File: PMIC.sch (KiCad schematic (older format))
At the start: 63 parts

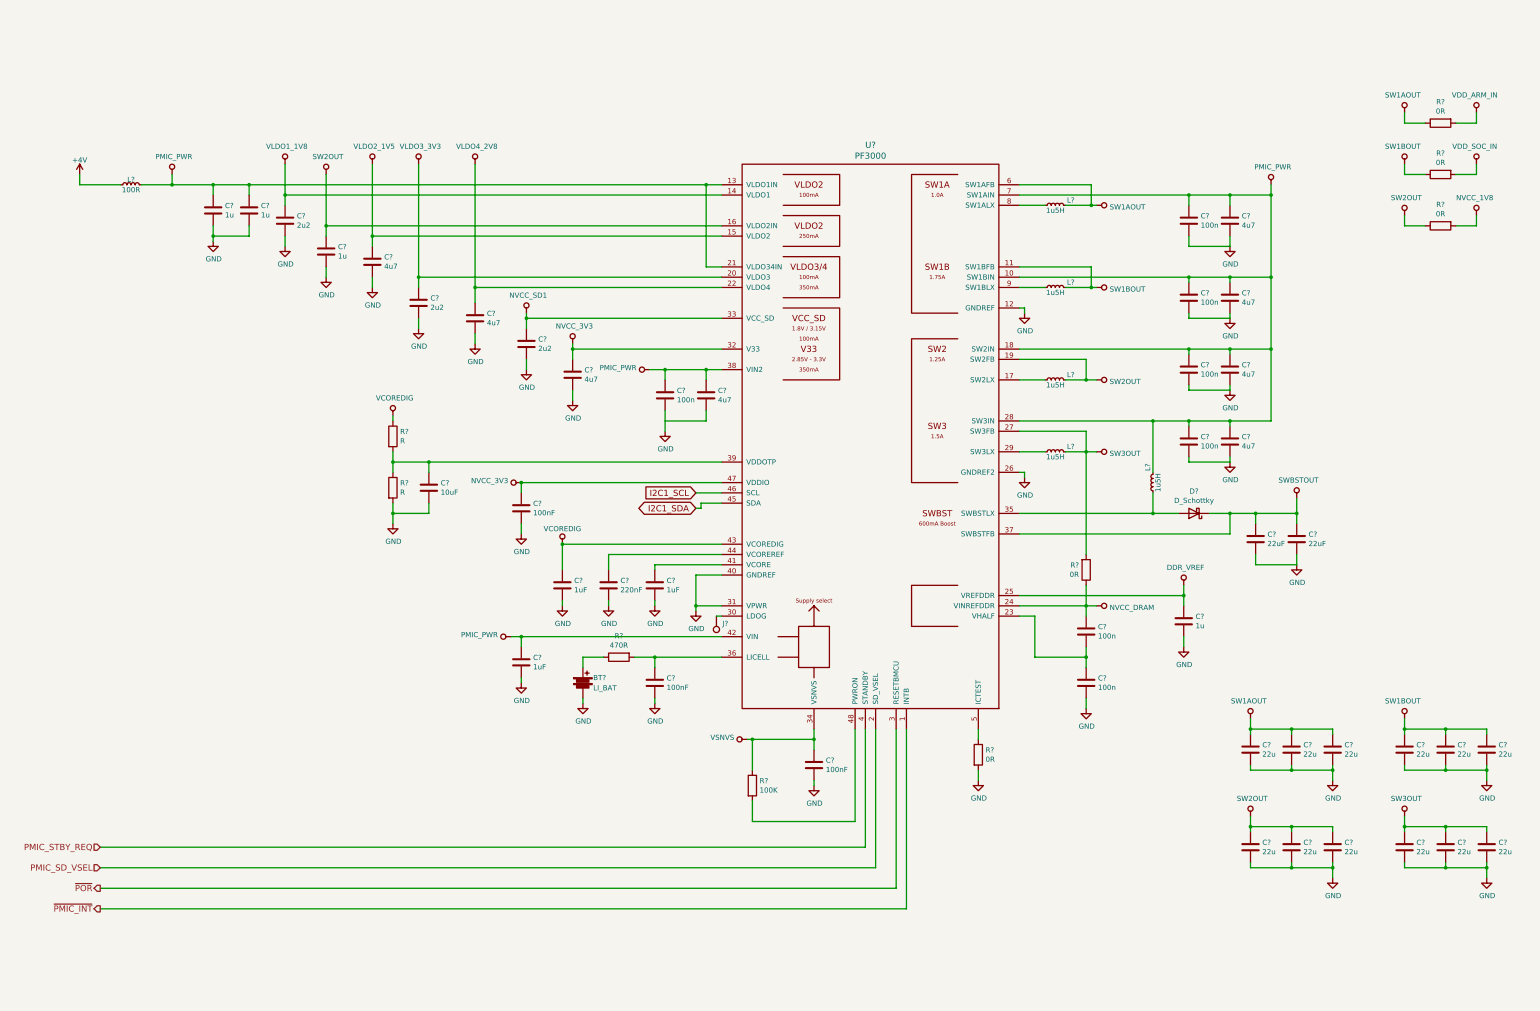
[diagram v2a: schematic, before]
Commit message: Prepare for two battery types NiMH battery for using the original battery pack LiPo battery for using long lasting modern battery
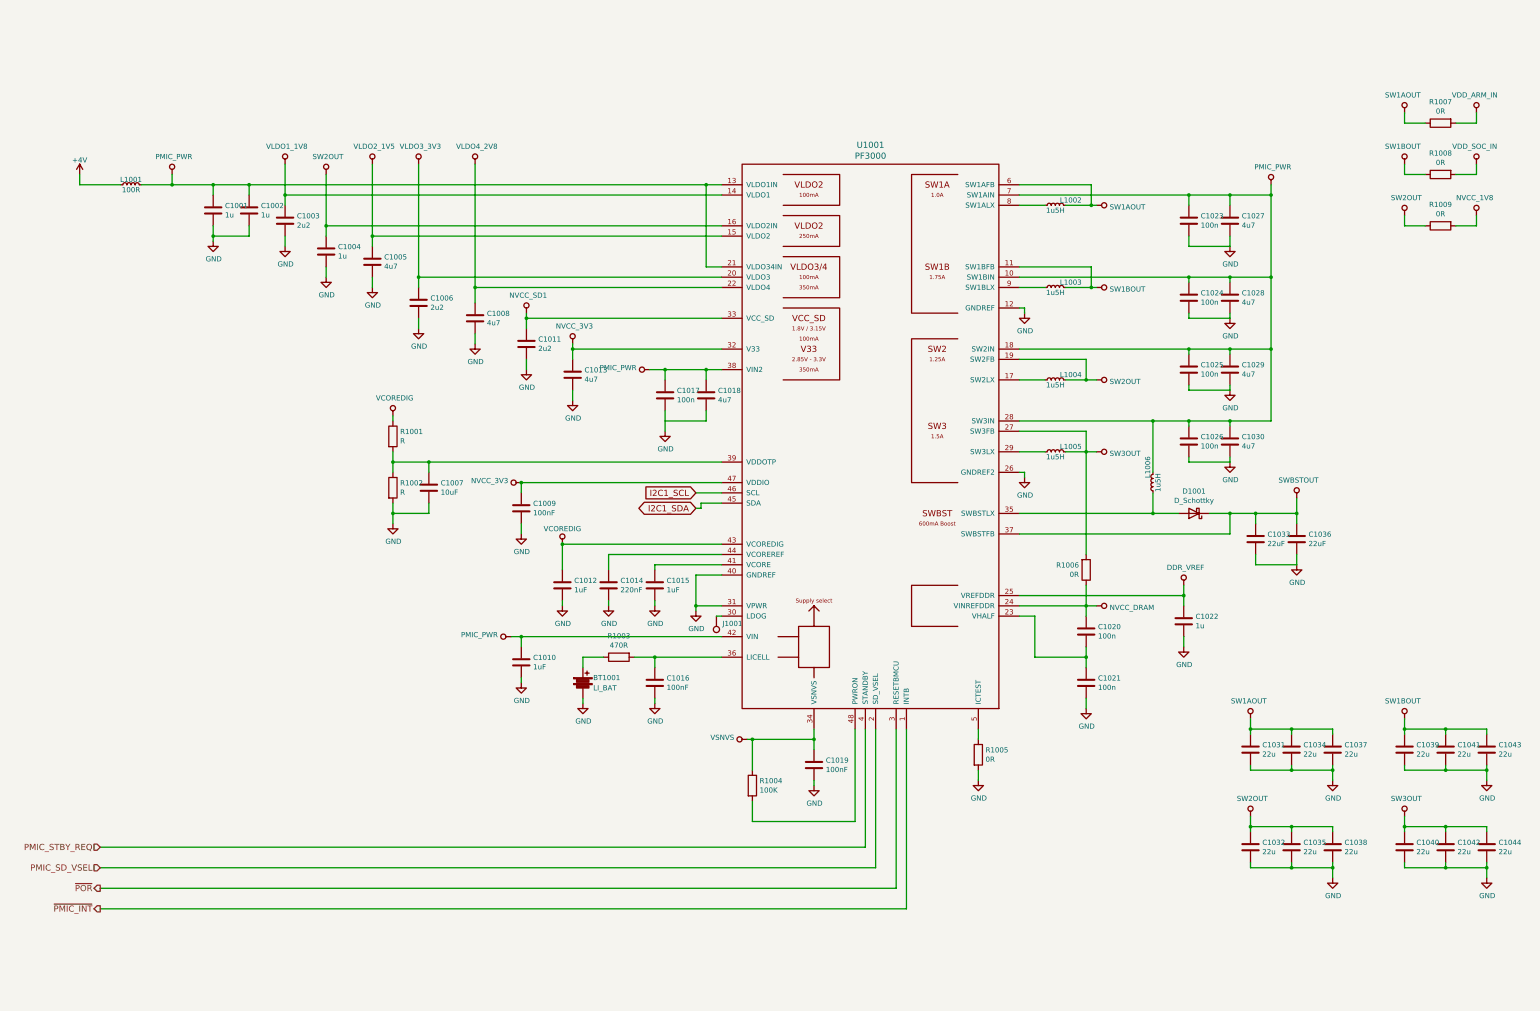
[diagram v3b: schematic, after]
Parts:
- gave numbers to parts that had none: 63

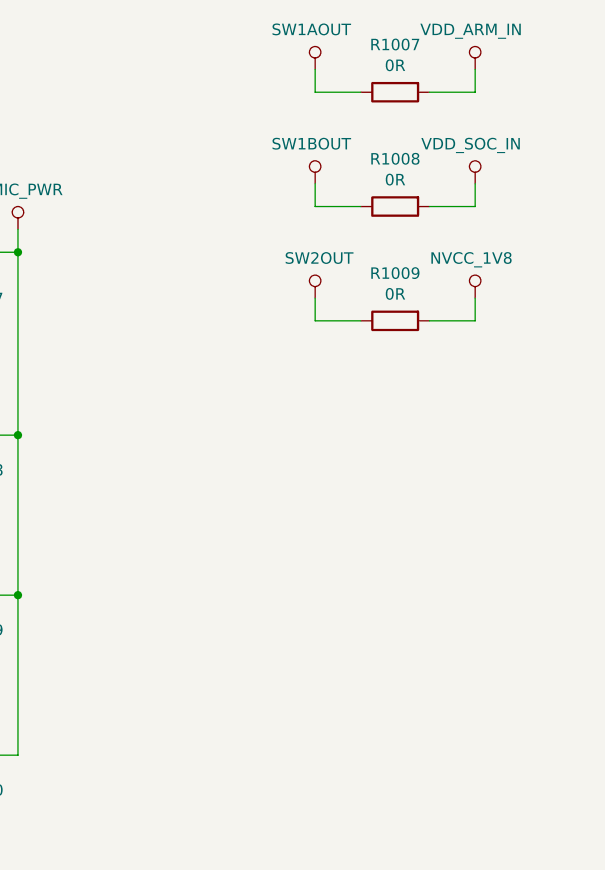
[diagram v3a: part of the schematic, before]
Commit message: Added power domains overview in POWER.sch subsheet fixed some power connections added datasheet for bq24401 charge controller updated schematic library
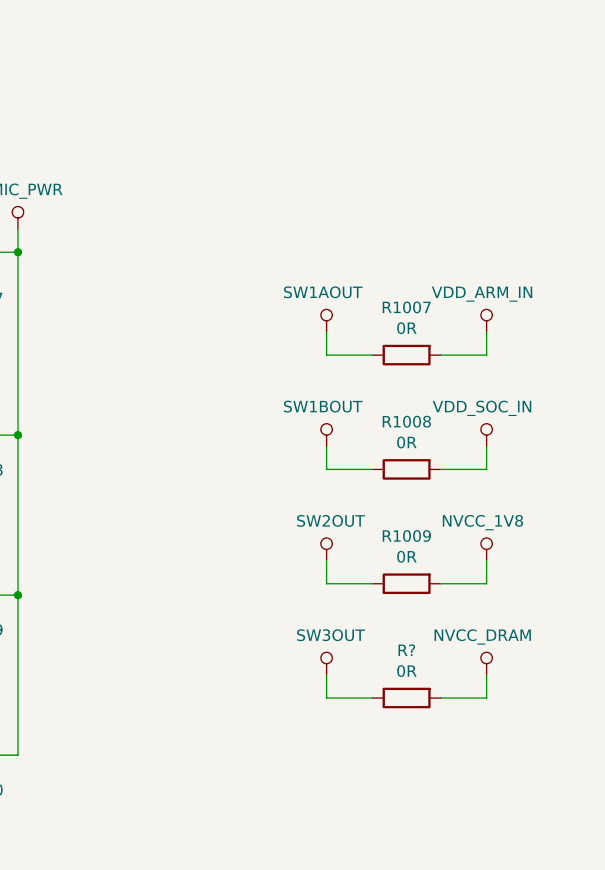
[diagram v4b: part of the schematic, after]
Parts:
- added R?: 0R, symbol R
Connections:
- net NVCC_DRAM: now also R?.2
- net SW3OUT: now also R?.1
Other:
- moved on the sheet: R1007, R1008, R1009
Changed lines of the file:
@@
 L VDD_ARM_IN #PWR1062
 U 1 1 59281B8F
-P 15300 1900
-F 0 "#PWR1062" H 15350 1950 50  0001 C CNN
-F 1 "VDD_ARM_IN" H 15317 2073 50  0000 C CNN
-F 2 "" H 6400 -750 50  0001 C CNN
-F 3 "" H 6400 -750 50  0001 C CNN
-	1    15300 1900
+P 15350 3050
+F 0 "#PWR1062" H 15400 3100 50  0001 C CNN
+F 1 "VDD_ARM_IN" H 15367 3223 50  0000 C CNN
+F 2 "" H 6450 400 50  0001 C CNN
+F 3 "" H 6450 400 50  0001 C CNN
+	1    15350 3050
 	-1   0    0    -1
 $EndComp
@@
 L VDD_SOC_IN #PWR1063
 U 1 1 5928223D
-P 15300 2400
-F 0 "#PWR1063" H 15350 2450 50  0001 C CNN
-F 1 "VDD_SOC_IN" H 15317 2573 50  0000 C CNN
-F 2 "" H 6400 -250 50  0001 C CNN
-F 3 "" H 6400 -250 50  0001 C CNN
-	1    15300 2400
+P 15350 3550
+F 0 "#PWR1063" H 15400 3600 50  0001 C CNN
+F 1 "VDD_SOC_IN" H 15367 3723 50  0000 C CNN
+F 2 "" H 6450 900 50  0001 C CNN
+F 3 "" H 6450 900 50  0001 C CNN
+	1    15350 3550
 	-1   0    0    -1
 $EndComp
@@
 L SW1AOUT #PWR1057
 U 1 1 593E805C
-P 14600 1900
-F 0 "#PWR1057" H 14650 1950 50  0001 C CNN
-F 1 "SW1AOUT" H 14617 2073 50  0000 C CNN
-F 2 "" H 2650 -1150 50  0001 C CNN
-F 3 "" H 2650 -1150 50  0001 C CNN
-	1    14600 1900
+P 14650 3050
+F 0 "#PWR1057" H 14700 3100 50  0001 C CNN
+F 1 "SW1AOUT" H 14667 3223 50  0000 C CNN
+F 2 "" H 2700 0   50  0001 C CNN
+F 3 "" H 2700 0   50  0001 C CNN
+	1    14650 3050
 	-1   0    0    -1
 $EndComp
@@
 L R R1007
 U 1 1 593E86B0
-P 14950 2000
-F 0 "R1007" V 14743 2000 50  0000 C CNN
-F 1 "0R" V 14834 2000 50  0000 C CNN
-F 2 "" V -20 -600 50  0001 C CNN
-F 3 "" H 50  -600 50  0001 C CNN
-	1    14950 2000
+P 15000 3150
+F 0 "R1007" V 14793 3150 50  0000 C CNN
+F 1 "0R" V 14884 3150 50  0000 C CNN
+F 2 "" V 30  550 50  0001 C CNN
+F 3 "" H 100 550 50  0001 C CNN
+	1    15000 3150
 	0    -1   1    0
 $EndComp
 Wire Wire Line
-	14800 2000 14600 2000
-Wire Wire Line
-	14600 2000 14600 1900
-Wire Wire Line
-	15100 2000 15300 2000
-Wire Wire Line
-	15300 2000 15300 1900
+	14850 3150 14650 3150
+Wire Wire Line
+	14650 3150 14650 3050
+Wire Wire Line
+	15150 3150 15350 3150
+Wire Wire Line
+	15350 3150 15350 3050
 Wire Wire Line
 	11550 3400 11550 3600
@@
 L R R1008
 U 1 1 593E95E8
-P 14950 2500
-F 0 "R1008" V 14743 2500 50  0000 C CNN
-F 1 "0R" V 14834 2500 50  0000 C CNN
-F 2 "" V -20 -100 50  0001 C CNN
-F 3 "" H 50  -100 50  0001 C CNN
-	1    14950 2500
+P 15000 3650
+F 0 "R1008" V 14793 3650 50  0000 C CNN
+F 1 "0R" V 14884 3650 50  0000 C CNN
+F 2 "" V 30  1050 50  0001 C CNN
+F 3 "" H 100 1050 50  0001 C CNN
+	1    15000 3650
 	0    -1   1    0
 $EndComp
 Wire Wire Line
-	14800 2500 14600 2500
-Wire Wire Line
-	14600 2500 14600 2400
-Wire Wire Line
-	15100 2500 15300 2500
-Wire Wire Line
-	15300 2500 15300 2400
+	14850 3650 14650 3650
+Wire Wire Line
+	14650 3650 14650 3550
+Wire Wire Line
+	15150 3650 15350 3650
+Wire Wire Line
+	15350 3650 15350 3550
 $Comp
 L SW1BOUT #PWR1058
 U 1 1 593E967C
-P 14600 2400
-F 0 "#PWR1058" H 14650 2450 50  0001 C CNN
-F 1 "SW1BOUT" H 14617 2573 50  0000 C CNN
-F 2 "" H 2900 -1250 50  0001 C CNN
-F 3 "" H 2900 -1250 50  0001 C CNN
-	1    14600 2400
+P 14650 3550
+F 0 "#PWR1058" H 14700 3600 50  0001 C CNN
+F 1 "SW1BOUT" H 14667 3723 50  0000 C CNN
+F 2 "" H 2950 -100 50  0001 C CNN
+F 3 "" H 2950 -100 50  0001 C CNN
+	1    14650 3550
 	-1   0    0    -1
 $EndComp
@@
 L NVCC_1V8 #PWR1064
 U 1 1 593E9AC0
-P 15300 2900
-F 0 "#PWR1064" H 15350 2950 50  0001 C CNN
-F 1 "NVCC_1V8" H 15317 3073 50  0000 C CNN
-F 2 "" H 1300 800 50  0001 C CNN
-F 3 "" H 1300 800 50  0001 C CNN
-	1    15300 2900
+P 15350 4050
+F 0 "#PWR1064" H 15400 4100 50  0001 C CNN
+F 1 "NVCC_1V8" H 15367 4223 50  0000 C CNN
+F 2 "" H 1350 1950 50  0001 C CNN
+F 3 "" H 1350 1950 50  0001 C CNN
+	1    15350 4050
 	-1   0    0    -1
 $EndComp
@@
 L SW2OUT #PWR1059
 U 1 1 593E9BEA
-P 14600 2900
-F 0 "#PWR1059" H 14650 2950 50  0001 C CNN
-F 1 "SW2OUT" H 14617 3073 50  0000 C CNN
-F 2 "" H 2850 -1600 50  0001 C CNN
-F 3 "" H 2850 -1600 50  0001 C CNN
-	1    14600 2900
+P 14650 4050
+F 0 "#PWR1059" H 14700 4100 50  0001 C CNN
+F 1 "SW2OUT" H 14667 4223 50  0000 C CNN
+F 2 "" H 2900 -450 50  0001 C CNN
+F 3 "" H 2900 -450 50  0001 C CNN
+	1    14650 4050
 	1    0    0    -1
 $EndComp
@@
 L R R1009
 U 1 1 593E9DDD
-P 14950 3000
-F 0 "R1009" V 14743 3000 50  0000 C CNN
-F 1 "0R" V 14834 3000 50  0000 C CNN
-F 2 "" V -20 400 50  0001 C CNN
-F 3 "" H 50  400 50  0001 C CNN
-	1    14950 3000
+P 15000 4150
+F 0 "R1009" V 14793 4150 50  0000 C CNN
+F 1 "0R" V 14884 4150 50  0000 C CNN
+F 2 "" V 30  1550 50  0001 C CNN
+F 3 "" H 100 1550 50  0001 C CNN
+	1    15000 4150
 	0    -1   1    0
 $EndComp
 Wire Wire Line
-	14800 3000 14600 3000
-Wire Wire Line
-	14600 3000 14600 2900
-Wire Wire Line
-	15100 3000 15300 3000
-Wire Wire Line
-	15300 3000 15300 2900
+	14850 4150 14650 4150
+Wire Wire Line
+	14650 4150 14650 4050
+Wire Wire Line
+	15150 4150 15350 4150
+Wire Wire Line
+	15350 4150 15350 4050
 $Comp
 L C C1031
@@
 	1    0    0    -1
 $EndComp
+$Comp
+L NVCC_DRAM #PWR?
+U 1 1 5959870A
+P 15350 4550
+F 0 "#PWR?" H 15400 4600 50  0001 C CNN
+F 1 "NVCC_DRAM" H 15367 4723 50  0000 C CNN
+F 2 "" H 1350 2450 50  0001 C CNN
+F 3 "" H 1350 2450 50  0001 C CNN
+	1    15350 4550
+	-1   0    0    -1
+$EndComp
+$Comp
+L SW3OUT #PWR?
+U 1 1 59598710
+P 14650 4550
+F 0 "#PWR?" H 14700 4600 50  0001 C CNN
+F 1 "SW3OUT" H 14667 4723 50  0000 C CNN
+F 2 "" H 2900 50  50  0001 C CNN
+F 3 "" H 2900 50  50  0001 C CNN
+	1    14650 4550
+	1    0    0    -1
+$EndComp
+$Comp
+L R R?
+U 1 1 59598716
+P 15000 4650
+F 0 "R?" V 14793 4650 50  0000 C CNN
+F 1 "0R" V 14884 4650 50  0000 C CNN
+F 2 "" V 30  2050 50  0001 C CNN
+F 3 "" H 100 2050 50  0001 C CNN
+	1    15000 4650
+	0    -1   1    0
+$EndComp
+Wire Wire Line
+	14850 4650 14650 4650
+Wire Wire Line
+	14650 4650 14650 4550
+Wire Wire Line
+	15150 4650 15350 4650
+Wire Wire Line
+	15350 4650 15350 4550
 $EndSCHEMATC

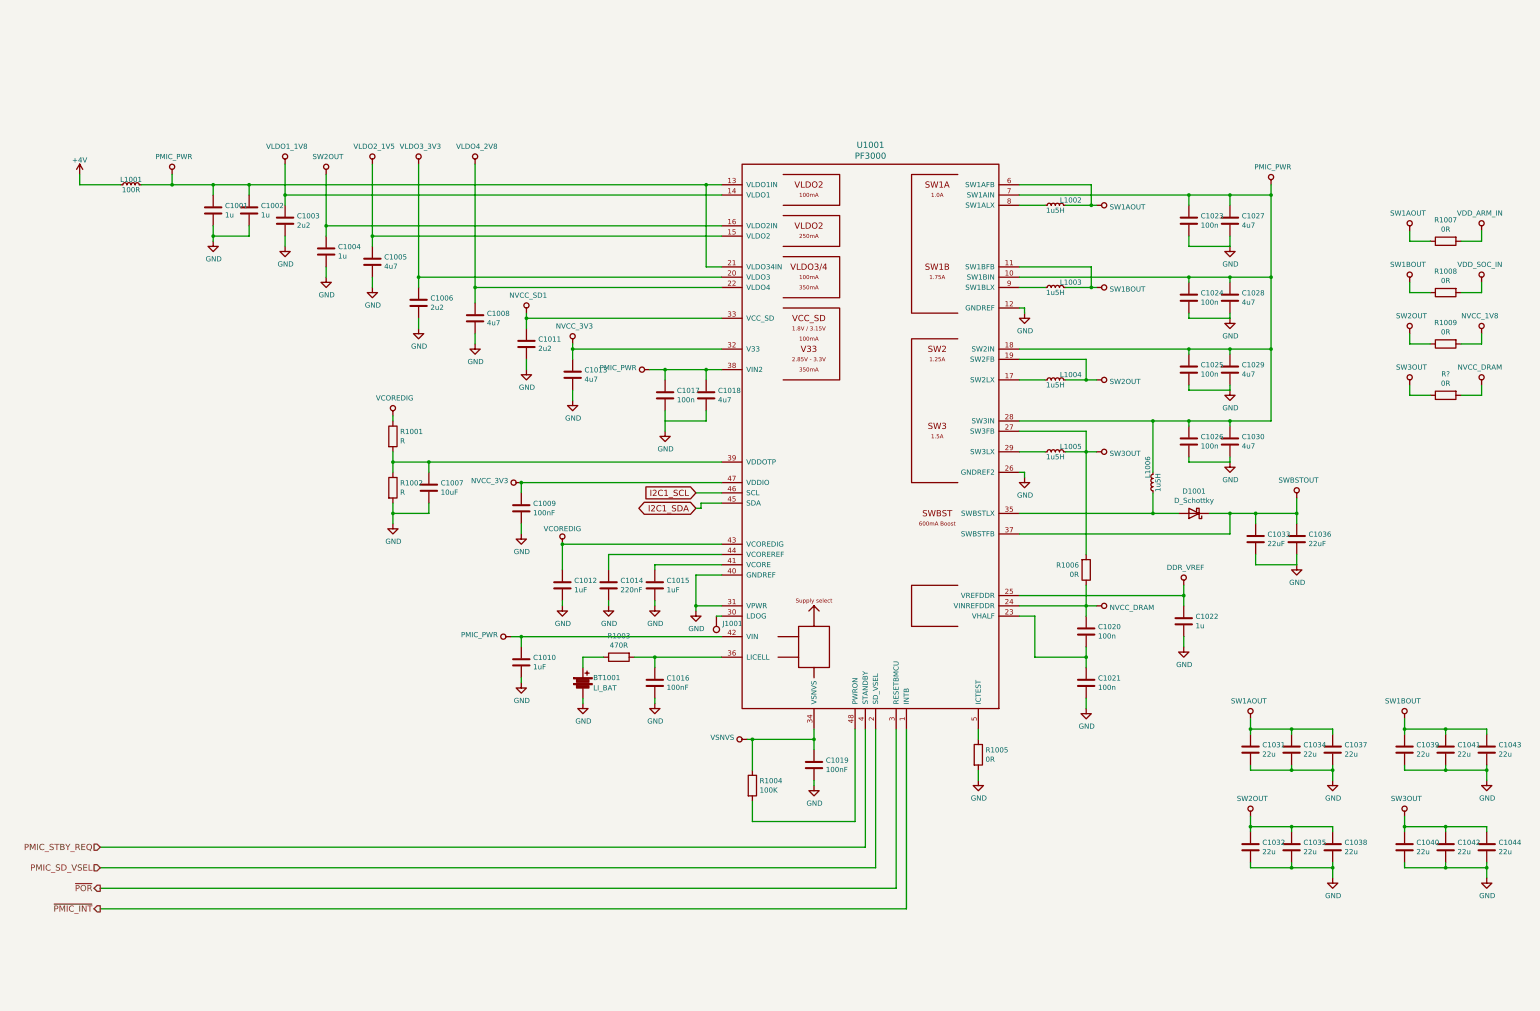
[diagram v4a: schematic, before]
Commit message: Modified power nets Added table of contents
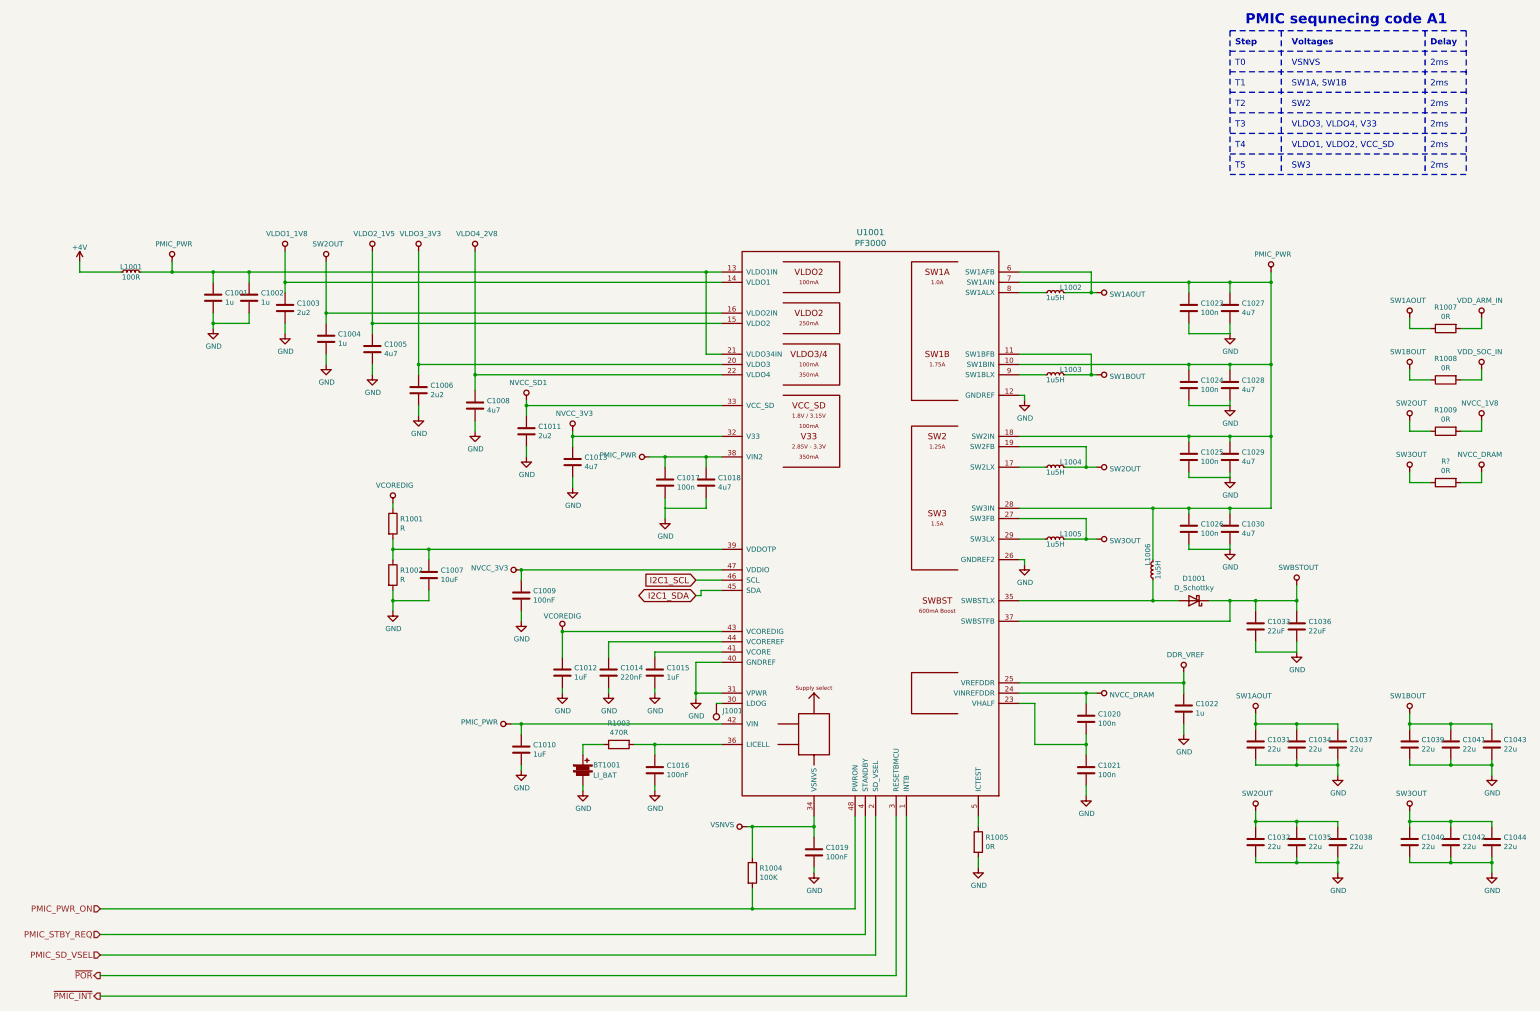
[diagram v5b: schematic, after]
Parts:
- removed R1006: 0R, symbol R
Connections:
- net PMIC_PWR_ON: now reaches R1004.2, U1001.48 (PWRON)
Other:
- note added: "2ms"
- note added: "Delay"
- note added: "PMIC sequnecing code A1"
- note added: "SW1A, SW1B"
- note added: "SW2"
- note added: "SW3"
- note added: "Step"
- note added: "T0"
- note added: "T1"
- note added: "T2"
- note added: "T3"
- note added: "T4"
- note added: "T5"
- note added: "VLDO1, VLDO2, VCC_SD"
- note added: "VLDO3, VLDO4, V33"
- note added: "VSNVS"
- note added: "Voltages"
- moved on the sheet: BT1001, C1001, C1002, C1003, C1004, C1005, C1006, C1007, C1008, C1009, C1010, C1011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
